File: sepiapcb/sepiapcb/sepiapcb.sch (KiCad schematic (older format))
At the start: 6 parts, among them SW1 SW_DPDT_x2

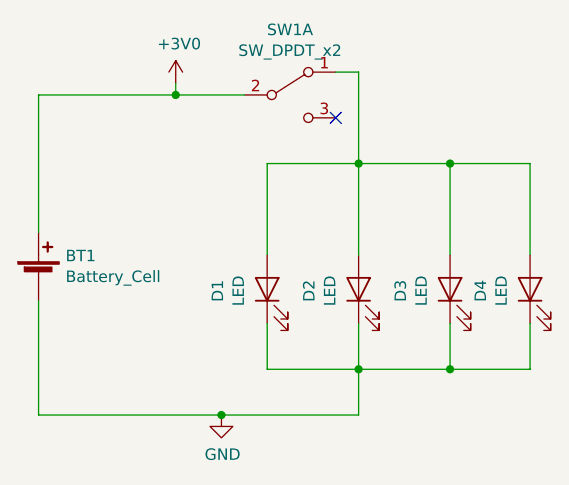
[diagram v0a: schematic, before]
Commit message: New sepia footprint with pads for THT leds, zone fills for both sides
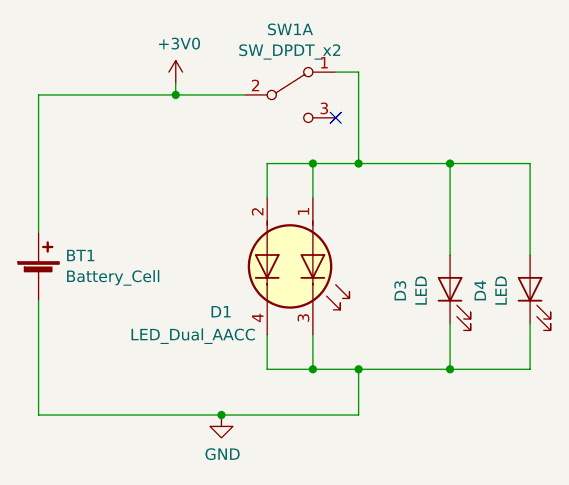
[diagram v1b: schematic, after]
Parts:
- removed D1, D2: LED, LED_SMD:LED_1206_3216Metric_Pad1.42x1.75mm_HandSolder, symbol Device:LED
- added D1: LED_Dual_AACC, sepiapcb:sepia_footrprint_pcb, symbol Device:LED_Dual_AACC
- D3, D4: footprint LED_THT:LED_D5.0mm_Horizontal_O1.27mm_Z3.0mm -> LED_SMD:LED_1206_3216Metric_Pad1.42x1.75mm_HandSolder
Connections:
- net GND: now also D1.3 (K1), D1.4 (K2)
- net at D3.2 (A), D4.2 (A), SW1.1 (A): now also D1.1 (A1), D1.2 (A2)
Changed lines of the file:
@@
-$EndComp
-$Comp
-L Device:LED D2
-U 1 1 5CFE94A7
-P 4600 2500
-F 0 "D2" H 4593 2716 50  0000 C CNN
-F 1 "LED" H 4593 2625 50  0000 C CNN
-F 2 "LED_SMD:LED_1206_3216Metric_Pad1.42x1.75mm_HandSolder" H 4600 2500 50  0001 C CNN
-F 3 "~" H 4600 2500 50  0001 C CNN
-	1    4600 2500
-	0    -1   -1   0
-$EndComp
-$Comp
-L Device:LED D1
-U 1 1 5CFF1212
-P 4200 2500
-F 0 "D1" H 4193 2716 50  0000 C CNN
-F 1 "LED" H 4193 2625 50  0000 C CNN
-F 2 "LED_SMD:LED_1206_3216Metric_Pad1.42x1.75mm_HandSolder" H 4200 2500 50  0001 C CNN
-F 3 "~" H 4200 2500 50  0001 C CNN
-	1    4200 2500
-	0    -1   -1   0
 $EndComp
 $Comp
@@
 F 0 "D4" H 5343 2716 50  0000 C CNN
 F 1 "LED" H 5343 2625 50  0000 C CNN
-F 2 "LED_THT:LED_D5.0mm_Horizontal_O1.27mm_Z3.0mm" H 5350 2500 50  0001 C CNN
+F 2 "LED_SMD:LED_1206_3216Metric_Pad1.42x1.75mm_HandSolder" H 5350 2500 50  0001 C CNN
 F 3 "~" H 5350 2500 50  0001 C CNN
 	1    5350 2500
@@
 F 0 "D3" H 4993 2716 50  0000 C CNN
 F 1 "LED" H 4993 2625 50  0000 C CNN
-F 2 "LED_THT:LED_D5.0mm_Horizontal_O1.27mm_Z3.0mm" H 5000 2500 50  0001 C CNN
+F 2 "LED_SMD:LED_1206_3216Metric_Pad1.42x1.75mm_HandSolder" H 5000 2500 50  0001 C CNN
 F 3 "~" H 5000 2500 50  0001 C CNN
 	1    5000 2500
@@
 Wire Wire Line
 	5000 1950 5350 1950
-Wire Wire Line
-	4200 2850 4200 2650
-Wire Wire Line
-	4600 2850 4600 2650
 Connection ~ 4600 2850
 Wire Wire Line
-	4600 2850 4200 2850
+	4600 2850 4400 2850
 Wire Wire Line
 	5000 2850 5000 2650
@@
 Wire Wire Line
 	4600 2850 5000 2850
-Wire Wire Line
-	4200 1950 4200 2350
 Connection ~ 5000 1950
-Wire Wire Line
-	4600 1950 4600 2350
 Connection ~ 4600 1950
 Wire Wire Line
 	4600 1950 5000 1950
 Wire Wire Line
-	4200 1950 4600 1950
+	4200 1950 4400 1950
 Wire Wire Line
 	4600 2850 4600 3050
@@
 NoConn ~ 4500 1750
 $Comp
-L power:GND #PWR?
+L power:GND #PWR0101
 U 1 1 5CFFD18A
 P 4000 3050
-F 0 "#PWR?" H 4000 2800 50  0001 C CNN
+F 0 "#PWR0101" H 4000 2800 50  0001 C CNN
 F 1 "GND" H 4005 2877 50  0000 C CNN
 F 2 "" H 4000 3050 50  0001 C CNN
@@
 	4000 3050 3200 3050
 $Comp
-L power:+3V0 #PWR?
+L power:+3V0 #PWR0102
 U 1 1 5CFFD583
 P 3800 1600
-F 0 "#PWR?" H 3800 1450 50  0001 C CNN
+F 0 "#PWR0102" H 3800 1450 50  0001 C CNN
 F 1 "+3V0" H 3815 1773 50  0000 C CNN
 F 2 "" H 3800 1600 50  0001 C CNN
@@
 Wire Wire Line
 	3800 1650 4100 1650
+$Comp
+L Device:LED_Dual_AACC D1
+U 1 1 5D017E85
+P 4300 2400
+F 0 "D1" V 4500 2050 50  0000 L CNN
+F 1 "LED_Dual_AACC" V 4600 1700 50  0000 L CNN
+F 2 "sepiapcb:sepia_footrprint_pcb" H 4330 2400 50  0001 C CNN
+F 3 "~" H 4330 2400 50  0001 C CNN
+	1    4300 2400
+	0    1    1    0
+$EndComp
+Wire Wire Line
+	4200 1950 4200 2100
+Wire Wire Line
+	4400 1950 4400 2100
+Connection ~ 4400 1950
+Wire Wire Line
+	4400 1950 4600 1950
+Wire Wire Line
+	4200 2700 4200 2850
+Wire Wire Line
+	4400 2700 4400 2850
+Connection ~ 4400 2850
+Wire Wire Line
+	4400 2850 4200 2850
 $EndSCHEMATC

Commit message: TH coin cell battery holder
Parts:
- BT1: footprint Battery:BatteryHolder_Keystone_3034_1x20mm -> Cell_Coin_Holders:Keystone_3003_CR2032_THT
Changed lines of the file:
@@
 F 0 "BT1" H 3318 2546 50  0000 L CNN
 F 1 "Battery_Cell" H 3318 2455 50  0000 L CNN
-F 2 "Battery:BatteryHolder_Keystone_3034_1x20mm" V 3200 2510 50  0001 C CNN
+F 2 "Cell_Coin_Holders:Keystone_3003_CR2032_THT" V 3200 2510 50  0001 C CNN
 F 3 "~" V 3200 2510 50  0001 C CNN
 	1    3200 2450
